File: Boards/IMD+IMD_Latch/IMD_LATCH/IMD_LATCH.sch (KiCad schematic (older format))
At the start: 32 parts, among them J1 UF_5_VT, J2 MM_F_RA_04, J3 MicroFit_V_2, K1 G5Q-1A4-DC5-5V, Q1 SSM3K333R, Q2 SSM3K333R, U1 TLV3701QDBVRG4Q1, U2 CD4043BPWR, U3 TLV3701QDBVRG4Q1

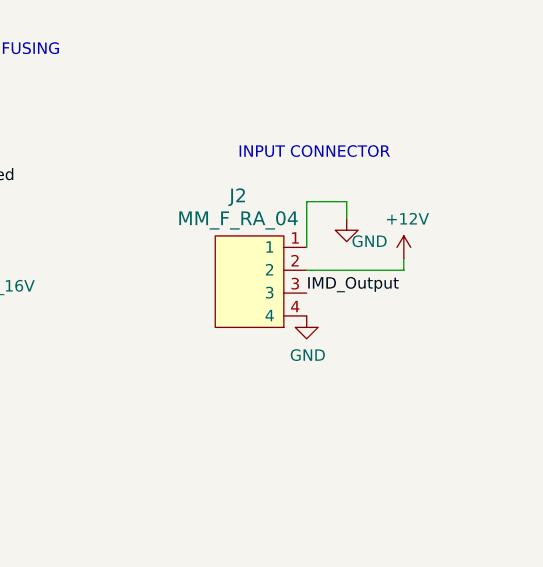
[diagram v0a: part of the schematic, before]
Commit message: Layout revision with updated connector placement and back layer.
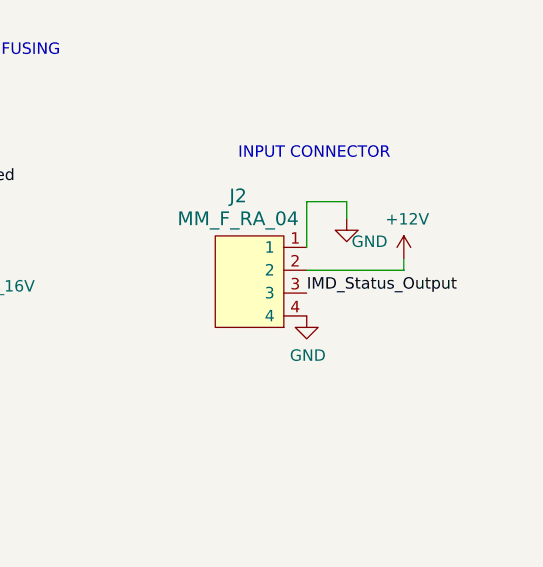
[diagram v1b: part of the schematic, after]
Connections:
- net IMD_Output: no longer J2.3
- net IMD_Status_Output: now also J2.3
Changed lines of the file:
@@
 $EndComp
 Text Label 10175 5900 0    50   ~ 0
-IMD_Output
+IMD_Status_Output
 $Comp
 L power:+12V #PWR011
